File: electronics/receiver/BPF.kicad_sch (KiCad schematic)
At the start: 26 parts

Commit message: TEST
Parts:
- C429: value C_Trim -> 5-22pF
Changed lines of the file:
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@@
       (effects (font (size 1.27 1.27)) (justify left))
     )
-    (property "Value" "C_Trim" (id 1) (at 89.3064 99.4026 0)
+    (property "Value" "5-22pF" (id 1) (at 89.3064 99.4026 0)
       (effects (font (size 1.27 1.27)) (justify left))
     )

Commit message: Filter
Filter values entered
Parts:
- C425: value C -> 15p
- C426, C430, C445: value C -> 6p8
- C427: value C -> 8p2
- C428: value C -> 18p
- C431: value C -> 0p7
- C432, C437, C442: value C -> 12p0
- C433, C438: value C -> 22p0
- C434, C439, C444: value C_Trim -> 5-22pF
- C435: value C -> 0p9
- C436, C441: value C -> 0p5
- C440: value C -> 1p8
- C443: value C -> 15p0
- C446: value C -> 3p9
- L403, L404, L405, L406: value L -> 54n6

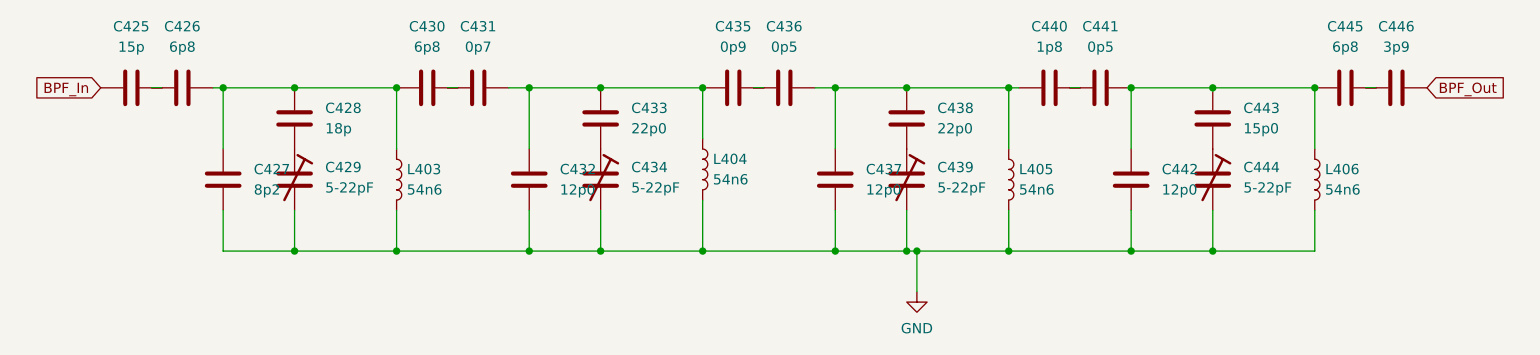
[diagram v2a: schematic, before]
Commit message: Branch for changes to RX LNA board from M0SKP
Upgrade files to Kicad 7
Added Fields for comment and LCSC part numbers to symbol table
Populated some LCSC part numbers to allow testing at JLCPCB
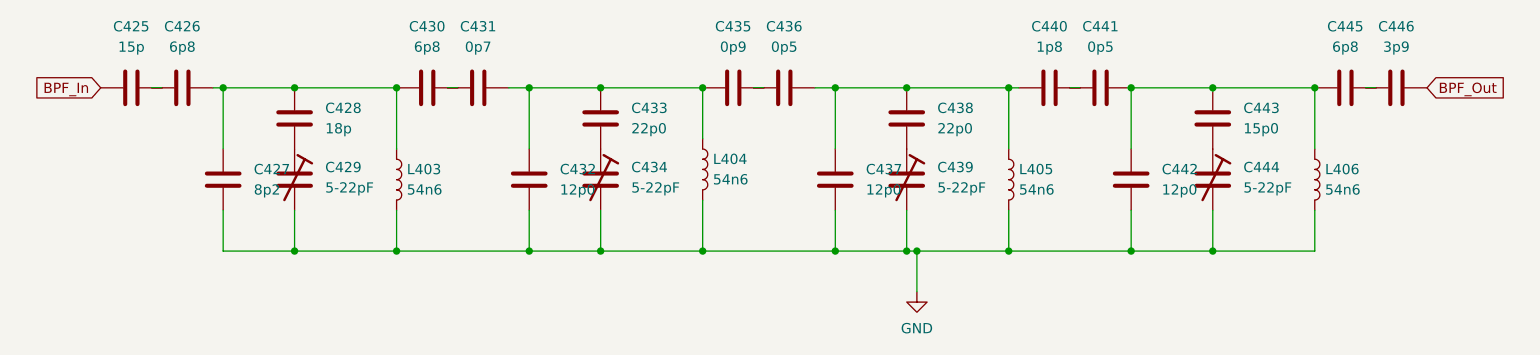
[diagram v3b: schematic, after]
